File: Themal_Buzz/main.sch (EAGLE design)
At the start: 12 parts

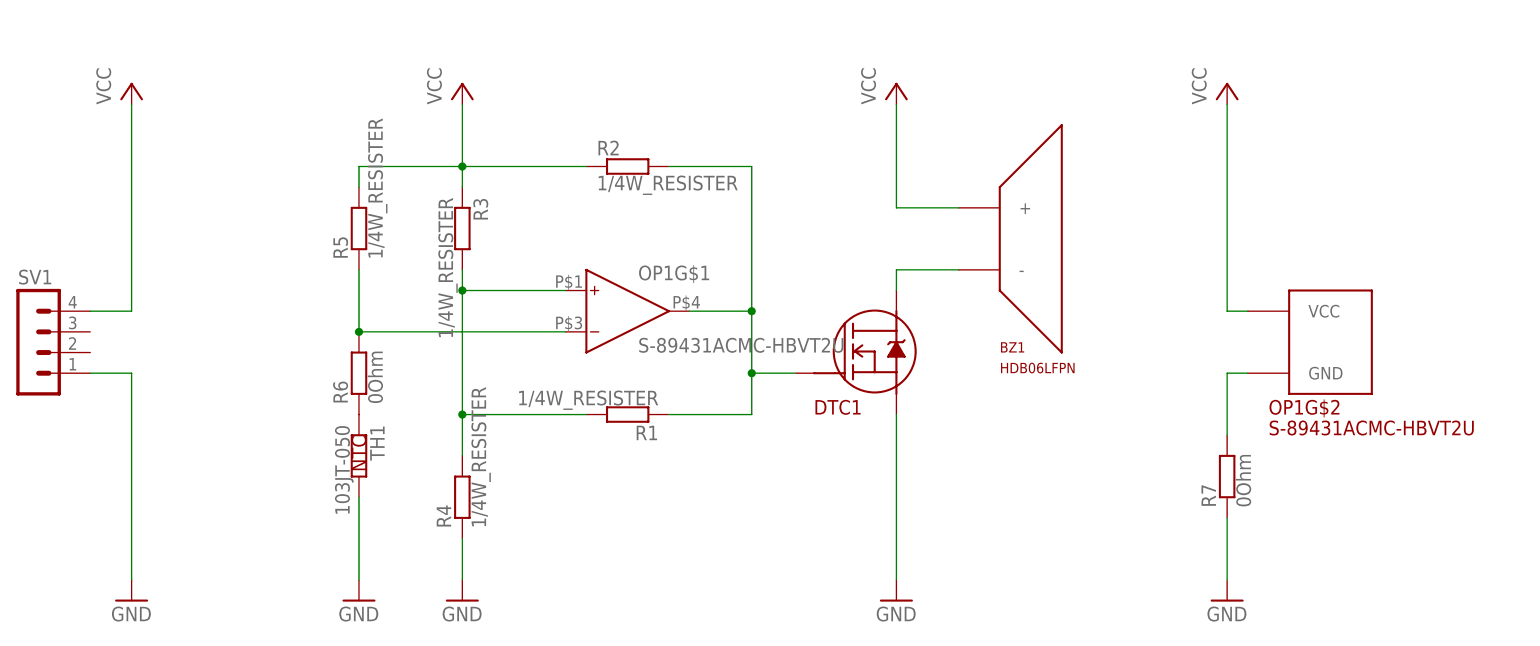
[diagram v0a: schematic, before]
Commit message: 抵抗値の設定完了
各抵抗値の設定完了
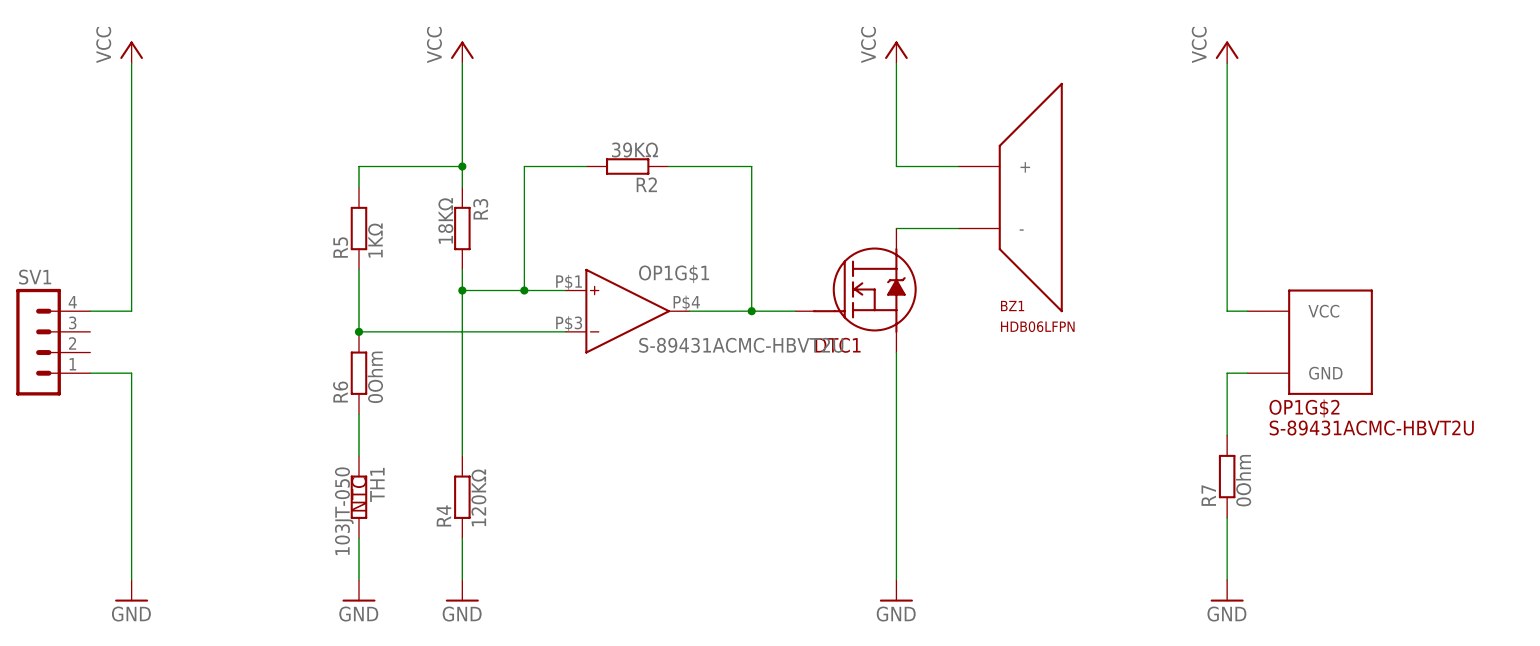
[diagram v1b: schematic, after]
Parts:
- removed R1: 1/4W_RESISTER, Tr_EXT:1/4W_RESISTER
- R2: value 1/4W_RESISTER -> 39KΩ
- R3: value 1/4W_RESISTER -> 18KΩ
- R4: value 1/4W_RESISTER -> 120KΩ
- R5: value 1/4W_RESISTER -> 1KΩ
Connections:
- removed net N$3: OP1G$1.IN+, R1.1, R3.1, R4.1
- new net N$7: OP1G$1.IN+, R2.1, R3.1, R4.1
- net N$1: now also R2.2; no longer R1.2, R2.1
- net VCC: no longer R2.2
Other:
- moved on the sheet: BZ1, DTC1, R2, TH1
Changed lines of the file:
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@@
 <part name="GND2" library="supply1" library_urn="urn:adsk.eagle:library:371" deviceset="GND" device=""/>
 <part name="GND3" library="supply1" library_urn="urn:adsk.eagle:library:371" deviceset="GND" device=""/>
-<part name="R1" library="Tr_EXT" deviceset="1/4W_RESISTER" device=""/>
-<part name="R2" library="Tr_EXT" deviceset="1/4W_RESISTER" device=""/>
-<part name="R3" library="Tr_EXT" deviceset="1/4W_RESISTER" device=""/>
-<part name="R4" library="Tr_EXT" deviceset="1/4W_RESISTER" device=""/>
-<part name="R5" library="Tr_EXT" deviceset="1/4W_RESISTER" device=""/>
+<part name="R2" library="Tr_EXT" deviceset="1/4W_RESISTER" device="" value="39KΩ"/>
+<part name="R3" library="Tr_EXT" deviceset="1/4W_RESISTER" device="" value="18KΩ"/>
+<part name="R4" library="Tr_EXT" deviceset="1/4W_RESISTER" device="" value="120KΩ"/>
+<part name="R5" library="Tr_EXT" deviceset="1/4W_RESISTER" device="" value="1KΩ"/>
 <part name="P+1" library="supply1" library_urn="urn:adsk.eagle:library:371" deviceset="VCC" device=""/>
 <part name="P+2" library="supply1" library_urn="urn:adsk.eagle:library:371" deviceset="VCC" device=""/>
@@
 <instance part="OP1" gate="G$1" x="129.54" y="99.06"/>
 <instance part="OP1" gate="G$2" x="213.36" y="101.6"/>
-<instance part="TH1" gate="G$1" x="99.06" y="81.28" rot="R270"/>
-<instance part="BZ1" gate="G$1" x="172.72" y="114.3"/>
+<instance part="TH1" gate="G$1" x="99.06" y="76.2" rot="R270"/>
+<instance part="BZ1" gate="G$1" x="172.72" y="119.38"/>
 <instance part="GND1" gate="1" x="165.1" y="63.5"/>
 <instance part="GND2" gate="1" x="205.74" y="63.5"/>
 <instance part="GND3" gate="1" x="99.06" y="63.5"/>
-<instance part="R1" gate="G$1" x="132.08" y="86.36" rot="R180"/>
-<instance part="R2" gate="G$1" x="132.08" y="116.84"/>
+<instance part="R2" gate="G$1" x="132.08" y="116.84" rot="R180"/>
 <instance part="R3" gate="G$1" x="111.76" y="109.22" rot="R270"/>
 <instance part="R4" gate="G$1" x="111.76" y="76.2" rot="R90"/>
 <instance part="R5" gate="G$1" x="99.06" y="109.22" rot="R90"/>
-<instance part="P+1" gate="VCC" x="111.76" y="127"/>
-<instance part="P+2" gate="VCC" x="205.74" y="127"/>
+<instance part="P+1" gate="VCC" x="111.76" y="132.08"/>
+<instance part="P+2" gate="VCC" x="205.74" y="132.08"/>
 <instance part="GND4" gate="1" x="111.76" y="63.5"/>
 <instance part="SV1" gate="1" x="58.42" y="96.52"/>
-<instance part="P+3" gate="VCC" x="71.12" y="127"/>
+<instance part="P+3" gate="VCC" x="71.12" y="132.08"/>
 <instance part="GND5" gate="1" x="71.12" y="63.5"/>
-<instance part="P+4" gate="VCC" x="165.1" y="127"/>
-<instance part="DTC1" gate="G$1" x="162.56" y="93.98"/>
+<instance part="P+4" gate="VCC" x="165.1" y="132.08"/>
+<instance part="DTC1" gate="G$1" x="162.56" y="101.6"/>
 <instance part="R6" gate="G$1" x="99.06" y="91.44" rot="R90"/>
 <instance part="R7" gate="G$1" x="205.74" y="78.74" rot="R90"/>
@@
 <segment>
 <pinref part="OP1" gate="G$1" pin="OUT"/>
-<pinref part="R2" gate="G$1" pin="1"/>
 <wire x1="147.32" y1="99.06" x2="139.7" y2="99.06" width="0.1524" layer="91"/>
-<wire x1="137.16" y1="116.84" x2="147.32" y2="116.84" width="0.1524" layer="91"/>
 <wire x1="147.32" y1="116.84" x2="147.32" y2="99.06" width="0.1524" layer="91"/>
 <junction x="147.32" y="99.06"/>
-<wire x1="147.32" y1="99.06" x2="147.32" y2="91.44" width="0.1524" layer="91"/>
-<pinref part="R1" gate="G$1" pin="2"/>
-<wire x1="147.32" y1="91.44" x2="147.32" y2="86.36" width="0.1524" layer="91"/>
-<wire x1="137.16" y1="86.36" x2="147.32" y2="86.36" width="0.1524" layer="91"/>
-<wire x1="152.654" y1="91.44" x2="147.32" y2="91.44" width="0.1524" layer="91"/>
-<junction x="147.32" y="91.44"/>
+<wire x1="152.654" y1="99.06" x2="147.32" y2="99.06" width="0.1524" layer="91"/>
 <pinref part="DTC1" gate="G$1" pin="G"/>
+<pinref part="R2" gate="G$1" pin="2"/>
+<wire x1="137.16" y1="116.84" x2="147.32" y2="116.84" width="0.1524" layer="91"/>
 </segment>
 </net>
@@
 <segment>
 <pinref part="GND1" gate="1" pin="GND"/>
-<wire x1="165.1" y1="86.36" x2="165.1" y2="66.04" width="0.1524" layer="91"/>
+<wire x1="165.1" y1="93.98" x2="165.1" y2="66.04" width="0.1524" layer="91"/>
 <pinref part="DTC1" gate="G$1" pin="S"/>
-</segment>
-<segment>
-<pinref part="TH1" gate="G$1" pin="1"/>
-<pinref part="GND3" gate="1" pin="GND"/>
-<wire x1="99.06" y1="76.2" x2="99.06" y2="66.04" width="0.1524" layer="91"/>
 </segment>
 <segment>
@@
 <wire x1="205.74" y1="66.04" x2="205.74" y2="73.66" width="0.1524" layer="91"/>
 </segment>
+<segment>
+<pinref part="GND3" gate="1" pin="GND"/>
+<pinref part="TH1" gate="G$1" pin="1"/>
+<wire x1="99.06" y1="66.04" x2="99.06" y2="71.12" width="0.1524" layer="91"/>
+</segment>
 </net>
 <net name="N$2" class="0">
@@
 <pinref part="OP1" gate="G$1" pin="IN-"/>
 <wire x1="99.06" y1="96.52" x2="124.46" y2="96.52" width="0.1524" layer="91"/>
+<pinref part="R6" gate="G$1" pin="1"/>
 <pinref part="R5" gate="G$1" pin="2"/>
-<wire x1="99.06" y1="104.14" x2="99.06" y2="96.52" width="0.1524" layer="91"/>
-<pinref part="R6" gate="G$1" pin="1"/>
+<wire x1="99.06" y1="96.52" x2="99.06" y2="104.14" width="0.1524" layer="91"/>
 <junction x="99.06" y="96.52"/>
-</segment>
-</net>
-<net name="N$3" class="0">
-<segment>
-<pinref part="R4" gate="G$1" pin="1"/>
-<pinref part="OP1" gate="G$1" pin="IN+"/>
-<wire x1="111.76" y1="81.28" x2="111.76" y2="86.36" width="0.1524" layer="91"/>
-<wire x1="111.76" y1="86.36" x2="111.76" y2="101.6" width="0.1524" layer="91"/>
-<wire x1="124.46" y1="101.6" x2="111.76" y2="101.6" width="0.1524" layer="91"/>
-<pinref part="R3" gate="G$1" pin="1"/>
-<wire x1="111.76" y1="104.14" x2="111.76" y2="101.6" width="0.1524" layer="91"/>
-<junction x="111.76" y="101.6"/>
-<pinref part="R1" gate="G$1" pin="1"/>
-<wire x1="127" y1="86.36" x2="111.76" y2="86.36" width="0.1524" layer="91"/>
-<junction x="111.76" y="86.36"/>
 </segment>
 </net>
 <net name="VCC" class="0">
 <segment>
-<pinref part="R2" gate="G$1" pin="2"/>
-<wire x1="127" y1="116.84" x2="111.76" y2="116.84" width="0.1524" layer="91"/>
+<pinref part="P+1" gate="VCC" pin="VCC"/>
+<junction x="111.76" y="116.84"/>
+<wire x1="111.76" y1="116.84" x2="111.76" y2="129.54" width="0.1524" layer="91"/>
+<pinref part="R3" gate="G$1" pin="2"/>
+<wire x1="111.76" y1="114.3" x2="111.76" y2="116.84" width="0.1524" layer="91"/>
+<wire x1="111.76" y1="116.84" x2="99.06" y2="116.84" width="0.1524" layer="91"/>
 <pinref part="R5" gate="G$1" pin="1"/>
 <wire x1="99.06" y1="114.3" x2="99.06" y2="116.84" width="0.1524" layer="91"/>
-<wire x1="111.76" y1="116.84" x2="99.06" y2="116.84" width="0.1524" layer="91"/>
-<junction x="111.76" y="116.84"/>
-<pinref part="P+1" gate="VCC" pin="VCC"/>
-<wire x1="111.76" y1="116.84" x2="111.76" y2="124.46" width="0.1524" layer="91"/>
-<pinref part="R3" gate="G$1" pin="2"/>
-<wire x1="111.76" y1="114.3" x2="111.76" y2="116.84" width="0.1524" layer="91"/>
 </segment>
 <segment>
 <pinref part="P+2" gate="VCC" pin="VCC"/>
 <pinref part="OP1" gate="G$2" pin="VCC"/>
-<wire x1="205.74" y1="124.46" x2="205.74" y2="99.06" width="0.1524" layer="91"/>
+<wire x1="205.74" y1="129.54" x2="205.74" y2="99.06" width="0.1524" layer="91"/>
 <wire x1="205.74" y1="99.06" x2="208.28" y2="99.06" width="0.1524" layer="91"/>
 </segment>
@@
 <pinref part="P+3" gate="VCC" pin="VCC"/>
 <wire x1="66.04" y1="99.06" x2="71.12" y2="99.06" width="0.1524" layer="91"/>
-<wire x1="71.12" y1="99.06" x2="71.12" y2="124.46" width="0.1524" layer="91"/>
+<wire x1="71.12" y1="99.06" x2="71.12" y2="129.54" width="0.1524" layer="91"/>
 </segment>
 <segment>
 <pinref part="BZ1" gate="G$1" pin="+"/>
 <pinref part="P+4" gate="VCC" pin="VCC"/>
-<wire x1="172.72" y1="111.76" x2="165.1" y2="111.76" width="0.1524" layer="91"/>
-<wire x1="165.1" y1="111.76" x2="165.1" y2="124.46" width="0.1524" layer="91"/>
+<wire x1="172.72" y1="116.84" x2="165.1" y2="116.84" width="0.1524" layer="91"/>
+<wire x1="165.1" y1="116.84" x2="165.1" y2="129.54" width="0.1524" layer="91"/>
 </segment>
 </net>
@@
 <segment>
 <pinref part="BZ1" gate="G$1" pin="-"/>
-<wire x1="172.72" y1="104.14" x2="165.1" y2="104.14" width="0.1524" layer="91"/>
-<wire x1="165.1" y1="104.14" x2="165.1" y2="101.6" width="0.1524" layer="91"/>
+<wire x1="172.72" y1="109.22" x2="165.1" y2="109.22" width="0.1524" layer="91"/>
 <pinref part="DTC1" gate="G$1" pin="D"/>
-</segment>
-</net>
-<net name="N$5" class="0">
-<segment>
-<pinref part="R6" gate="G$1" pin="2"/>
-<pinref part="TH1" gate="G$1" pin="2"/>
 </segment>
 </net>
@@
 </segment>
 </net>
+<net name="N$7" class="0">
+<segment>
+<pinref part="R4" gate="G$1" pin="1"/>
+<pinref part="OP1" gate="G$1" pin="IN+"/>
+<wire x1="111.76" y1="81.28" x2="111.76" y2="101.6" width="0.1524" layer="91"/>
+<wire x1="124.46" y1="101.6" x2="119.38" y2="101.6" width="0.1524" layer="91"/>
+<pinref part="R3" gate="G$1" pin="1"/>
+<wire x1="119.38" y1="101.6" x2="111.76" y2="101.6" width="0.1524" layer="91"/>
+<wire x1="111.76" y1="104.14" x2="111.76" y2="101.6" width="0.1524" layer="91"/>
+<junction x="111.76" y="101.6"/>
+<wire x1="119.38" y1="101.6" x2="119.38" y2="116.84" width="0.1524" layer="91"/>
+<junction x="119.38" y="101.6"/>
+<pinref part="R2" gate="G$1" pin="1"/>
+<wire x1="127" y1="116.84" x2="119.38" y2="116.84" width="0.1524" layer="91"/>
+</segment>
+</net>
+<net name="N$5" class="0">
+<segment>
+<pinref part="TH1" gate="G$1" pin="2"/>
+<pinref part="R6" gate="G$1" pin="2"/>
+<wire x1="99.06" y1="81.28" x2="99.06" y2="86.36" width="0.1524" layer="91"/>
+</segment>
+</net>
